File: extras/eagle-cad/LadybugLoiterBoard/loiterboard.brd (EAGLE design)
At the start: 27.5 x 48 mm, 7 parts

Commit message: More LadybugFC loiterboard work
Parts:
- added SMIRF: (no value), SparkFun-Connectors:1X04
- moved LBLFT 11.8 mm to (20.5, 10.0)
- moved LBRGT 11.8 mm to (38.5, 13.0)
- moved PMLFT 11.8 mm to (22.0, 36.3)
- moved PMRGT 11.8 mm to (37.5, 36.3)
- moved PWPWR 11.8 mm to (27.3, 43.8)
- moved VLLFT 11.8 mm to (22.0, 25.9)
- moved VLRGT2 11.8 mm to (37.5, 25.9)
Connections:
- net A4 renamed LED
- removed net TX2/INT: LBLFT.6, VLLFT.3
- new net INT: VLLFT.3
- new net TX2: LBLFT.6, SMIRF.1
- net 5V: now also SMIRF.4
- net GND: now also SMIRF.3
- net RX2: now also SMIRF.2
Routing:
- net TX2: track 0.00 -> 79.6 mm
- net RX2: track 0.00 -> 72.1 mm
- net 5V: track 0.00 -> 71.9 mm
- net TX2/INT: track 31.2 -> 0.00 mm
- net GND: track 1.73 -> 0.12 mm
- removed copper zone on layer 16, net GND
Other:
- board size 27.5 x 48 mm -> 52.1 x 63 mm
- board text added: "5V"
- board text added: "ADD LEDS!"
- board text added: "BLUESMIRF"
- board text added: "CS"
- board text added: "GND"
- board text added: "INT"
- board text added: "LED"
- board text added: "MISO"
- board text added: "MOSI"
- board text added: "RX2"
- board text added: "SCK"
- board text added: "SCL"
- board text added: "SDA"
- board text added: "TX1"
- board text added: "TX2"

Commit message: More Ladybug Loiterboard work
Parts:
- added PAD1, PAD10, PAD2, PAD3, PAD4, PAD5, PAD6, PAD7, PAD8, PAD9: (no value), wirepad:SMD1,27-2,54
- added U$1: 1X2, headers(2mm):1X2
- moved SMIRF 0.75 mm to (50.0, 59.5)
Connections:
- new net VBAT: PAD9.1, U$1.1
- net 5V: now also PAD1.1, PAD3.1, PAD5.1, PAD7.1
- net GND: now also PAD10.1, U$1.2
- net LED: now also PAD2.1, PAD4.1, PAD6.1, PAD8.1
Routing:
- net GND: track 0.12 -> 7.65 mm
- net VBAT: track 0.00 -> 5.22 mm
- net 5V: track 71.9 -> 72.7 mm
- net RX2: track 72.1 -> 72.7 mm
- net TX2: track 79.6 -> 80.2 mm
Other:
- board size 52.1 x 63 mm -> 52.1 x 66.8 mm
- board text added: "VBAT"
- board text removed: "ADD LEDS!"

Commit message: More Ladybug Loiterboard work
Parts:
- moved PAD1 10.8 mm to (15.0, 12.0)
- moved PAD2 10.8 mm to (12.0, 12.0)
- moved PAD5 10.3 mm to (15.0, 39.0)
- moved PAD3 8.81 mm to (49.8, 12.0)
- moved PAD4 8.81 mm to (52.8, 12.0)
- moved PAD6 5.55 mm to (12.0, 39.0)
- moved PAD7 4.51 mm to (49.8, 39.0)
- moved PAD8 4.51 mm to (52.8, 39.0)
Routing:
- net LED: track 0.00 -> 145.1 mm, vias 0 -> 1
- net 5V: track 72.7 -> 141.8 mm, vias 0 -> 1
- net D4/MISO: track 47.1 -> 48.5 mm, vias 0 -> 1
- net SCL: track 17.0 -> 16.4 mm
- net SDA: vias 0 -> 1
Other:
- board size 52.1 x 66.8 mm -> 44.6 x 66.8 mm

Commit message: More Ladybug Loiterboard work
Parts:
- PAD6: value (none) -> LED

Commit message: Completed loiterboard
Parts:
- moved U$1 0.50 mm to (38.5, 4.25)
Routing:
- net VBAT: track 5.22 -> 6.24 mm
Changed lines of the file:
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@@
 <setting verticaltext="up"/>
 </settings>
-<grid distance="0.25" unitdist="mm" unit="mm" style="lines" multiple="1" display="no" altdistance="5" altunitdist="mil" altunit="mil"/>
+<grid distance="0.003125" unitdist="mic" unit="mm" style="lines" multiple="1" display="no" altdistance="5" altunitdist="mil" altunit="mil"/>
 <layers>
 <layer number="1" name="Top" color="4" fill="1" visible="yes" active="yes"/>
@@
 <attribute name="VALUE" x="52.75" y="39" size="0.0254" layer="27"/>
 </element>
-<element name="U$1" library="headers(2mm)" package="1X2" value="1X2" x="38.5" y="3.75" smashed="yes" rot="R270"/>
+<element name="U$1" library="headers(2mm)" package="1X2" value="1X2" x="38.5" y="4.25" smashed="yes" rot="R270"/>
 <element name="PAD9" library="wirepad" package="SMD1,27-2,54" value="" x="43" y="3" smashed="yes" rot="R180">
 <attribute name="VALUE" x="43" y="3" size="0.0254" layer="27" rot="R180"/>
@@
 <contactref element="SMIRF" pad="4"/>
 <wire x1="49.75" y1="51.63" x2="49.75" y2="40.25" width="0.3048" layer="1"/>
-<wire x1="49.75" y1="9.5" x2="46.25" y2="6" width="0.3048" layer="1"/>
-<wire x1="46.25" y1="6" x2="21" y2="6" width="0.3048" layer="1"/>
+<wire x1="49.75" y1="9.5" x2="46.6311875" y2="6.3811875" width="0.3048" layer="1"/>
+<wire x1="46.6311875" y1="6.3811875" x2="20.966846875" y2="6.3811875" width="0.3048" layer="1"/>
 <contactref element="PAD1" pad="1"/>
 <contactref element="PAD3" pad="1"/>
@@
 <wire x1="15" y1="12" x2="15" y2="12.75" width="0" layer="19" extent="1-1"/>
 <wire x1="15" y1="11.25" x2="15" y2="12" width="0" layer="19" extent="1-1"/>
-<wire x1="21" y1="6" x2="20.5" y2="6" width="0" layer="19" extent="1-1"/>
+<wire x1="20.966846875" y1="6.3811875" x2="20.5" y2="6" width="0" layer="19" extent="1-1"/>
 <wire x1="49.75" y1="39" x2="49.75" y2="40.25" width="0" layer="19" extent="1-1"/>
 </signal>
@@
 <contactref element="U$1" pad="2"/>
 <contactref element="PAD10" pad="1"/>
-<wire x1="38.5" y1="2.75" x2="40" y2="1.25" width="0.3048" layer="1"/>
-<wire x1="40" y1="1.25" x2="44" y2="1.25" width="0.3048" layer="1"/>
-<wire x1="44" y1="1.25" x2="45" y2="2.25" width="0.3048" layer="1"/>
-<wire x1="38.5" y1="2.75" x2="38.5" y2="18" width="0" layer="19" extent="1-1"/>
+<wire x1="38.5" y1="3.25" x2="39.98861875" y2="1.265175" width="0.3048" layer="1"/>
+<wire x1="39.98861875" y1="1.265175" x2="44.015175" y2="1.265175" width="0.3048" layer="1"/>
+<wire x1="44.015175" y1="1.265175" x2="45" y2="2.25" width="0.3048" layer="1"/>
+<wire x1="38.456" y1="17.9936" x2="38.5" y2="3.25" width="0" layer="19" extent="1-1"/>
 <wire x1="20.5" y1="16" x2="38.456" y2="17.9936" width="0" layer="19" extent="1-1"/>
 <wire x1="29.82" y1="43.8" x2="22" y2="28.46" width="0" layer="19" extent="1-1"/>
@@
 <contactref element="U$1" pad="1"/>
 <contactref element="PAD9" pad="1"/>
-<wire x1="38.5" y1="4.75" x2="41.25" y2="4.75" width="0.3048" layer="1"/>
-<wire x1="41.25" y1="4.75" x2="43" y2="3" width="0.3048" layer="1"/>
+<wire x1="42.5" y1="3" x2="43" y2="3" width="0.3048" layer="1"/>
+<wire x1="38.5" y1="5.25" x2="40" y2="5.25" width="0.3048" layer="1"/>
+<wire x1="40" y1="5.25" x2="43" y2="2.25" width="0.3048" layer="1"/>
+<wire x1="43" y1="2.25" x2="43" y2="3" width="0" layer="19" extent="1-1"/>
 </signal>
 </signals>

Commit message: Updated Loiterboard
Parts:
- moved SMIRF 2.52 mm to (52.5, 59.5)
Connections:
- net GND: now also U$1.1; no longer U$1.2
- net VBAT: now also U$1.2; no longer U$1.1
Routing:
- net 5V: track 141.6 -> 132.8 mm
- net TX2: track 80.2 -> 82.4 mm
- net RX2: track 72.7 -> 74.9 mm
- net VBAT: track 6.24 -> 5.00 mm

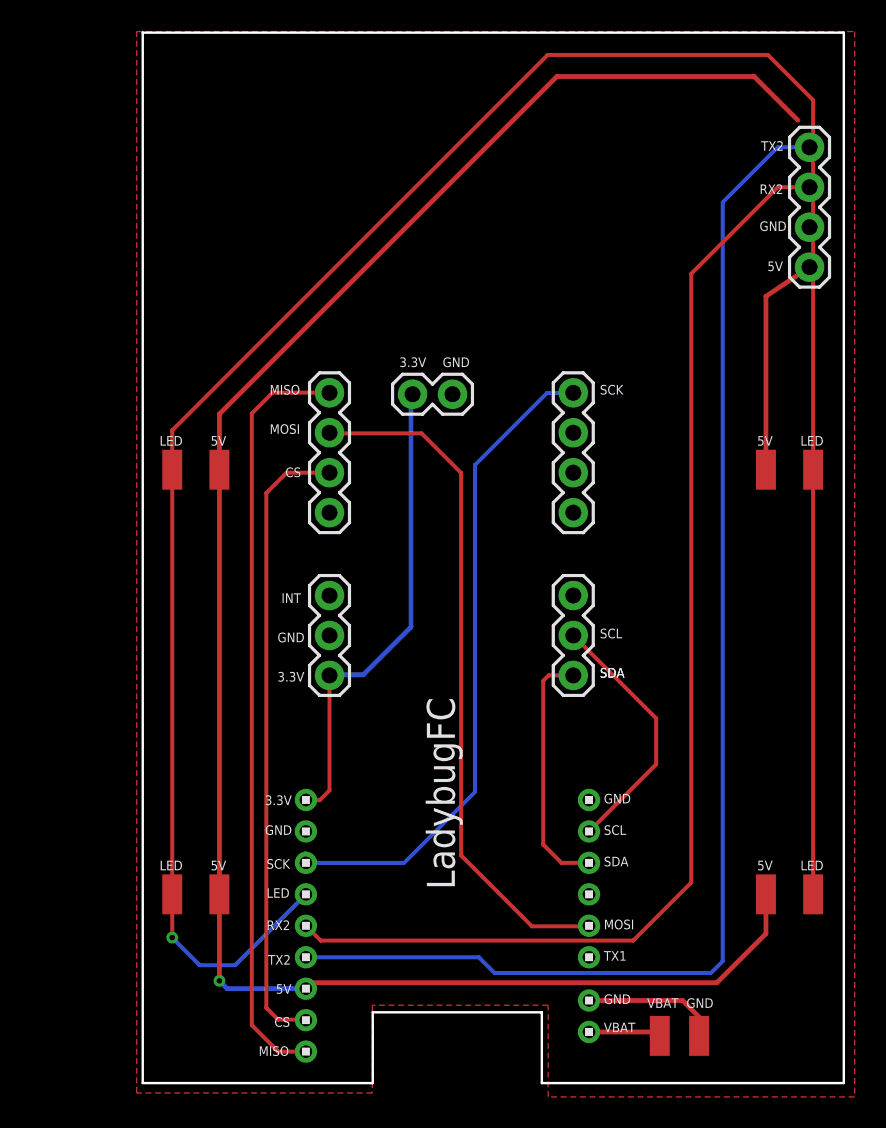
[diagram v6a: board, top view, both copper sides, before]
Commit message: Fixed 5V on loiterboard
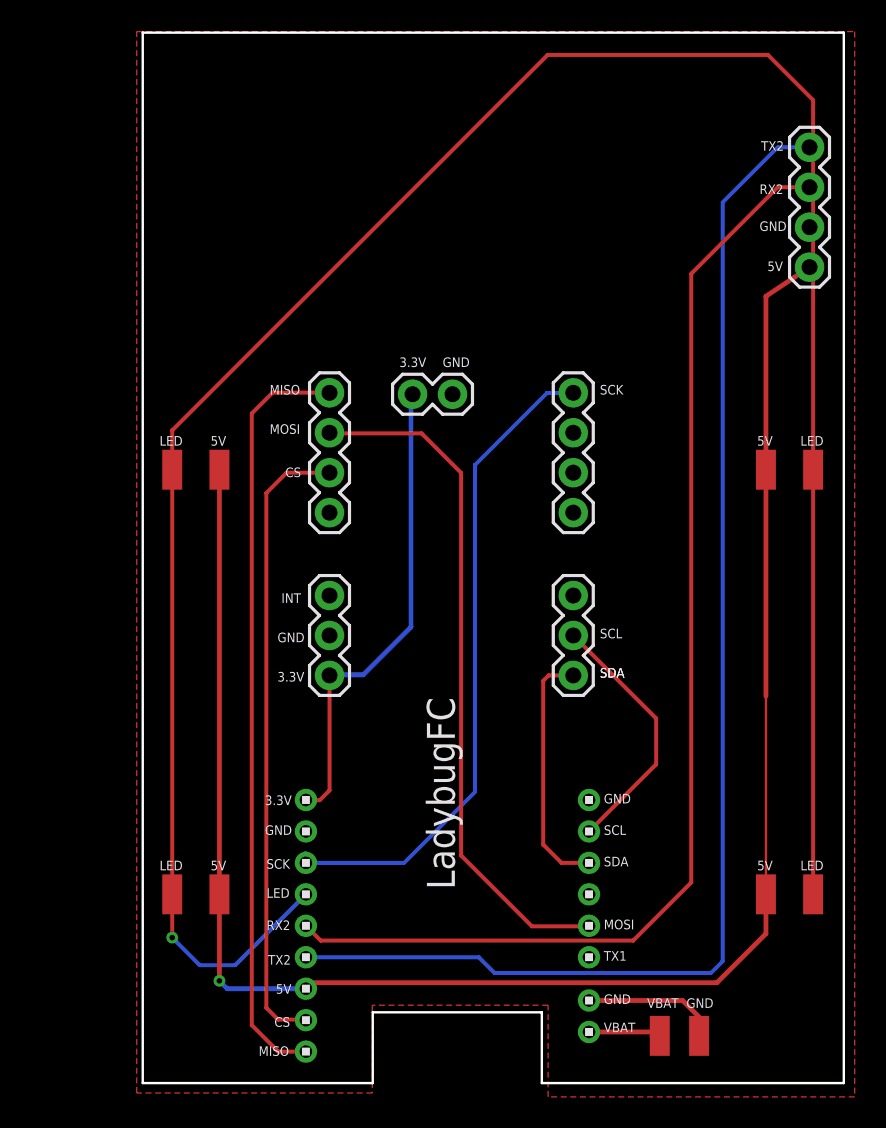
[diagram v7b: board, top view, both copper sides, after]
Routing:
- net 5V: track 132.8 -> 109.4 mm
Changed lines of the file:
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@@
 <contactref element="PAD5" pad="1"/>
 <contactref element="PAD7" pad="1"/>
-<wire x1="36.45763125" y1="64" x2="15" y2="42.54236875" width="0.3048" layer="1"/>
-<wire x1="36.45763125" y1="64" x2="49" y2="64" width="0.3048" layer="1"/>
-<wire x1="49" y1="64" x2="51.78231875" y2="61.21768125" width="0.3048" layer="1"/>
-<wire x1="15" y1="42.54236875" x2="15" y2="39" width="0.3048" layer="1"/>
 <wire x1="15" y1="39" x2="15" y2="12.75" width="0.3048" layer="1"/>
 <wire x1="20.5" y1="6" x2="15.5" y2="6" width="0.3048" layer="16"/>
@@
 <wire x1="49.75" y1="12" x2="49.75" y2="9.5" width="0.3048" layer="1"/>
 <wire x1="49.75" y1="50.025678125" x2="52.521875" y2="51.88" width="0.3048" layer="1"/>
+<wire x1="49.75" y1="39" x2="49.75" y2="24.6" width="0.3048" layer="1"/>
+<wire x1="49.75" y1="24.6" x2="49.75" y2="12" width="0.1524" layer="1"/>
 <wire x1="49.75" y1="39" x2="49.75" y2="40.25" width="0" layer="19" extent="1-1"/>
-<wire x1="51.78231875" y1="61.21768125" x2="52.521875" y2="51.88" width="0" layer="19" extent="1-1"/>
-<wire x1="15" y1="12" x2="15" y2="12.75" width="0" layer="19" extent="1-1"/>
-<wire x1="15" y1="11.25" x2="15" y2="12" width="0" layer="19" extent="1-1"/>
-<wire x1="20.966846875" y1="6.3811875" x2="20.5" y2="6" width="0" layer="19" extent="1-1"/>
+<wire x1="20.5" y1="6" x2="20.966846875" y2="6.3811875" width="0" layer="19" extent="1-1"/>
+<wire x1="15" y1="12" x2="15" y2="11.25" width="0" layer="19" extent="1-1"/>
+<wire x1="15" y1="12.75" x2="15" y2="12" width="0" layer="19" extent="1-1"/>
 </signal>
 <signal name="INT">
@@
 <wire x1="20.5" y1="16" x2="38.456" y2="17.9936" width="0" layer="19" extent="1-1"/>
 <wire x1="29.82" y1="43.8" x2="22" y2="28.46" width="0" layer="19" extent="1-1"/>
+<wire x1="52.521875" y1="54.42" x2="29.82" y2="43.8" width="0" layer="19" extent="1-1"/>
 </signal>
 <signal name="3.3V">

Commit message: More Loiterboard / Haskell Copilot work
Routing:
- net GND: track 7.76 -> 62.6 mm, vias 0 -> 1
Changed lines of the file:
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@@
 <wire x1="38.5" y1="5.25" x2="44.45" y2="5.25" width="0.3048" layer="1"/>
 <wire x1="44.45" y1="5.25" x2="45.7" y2="4" width="0.3048" layer="1"/>
+<wire x1="29.82" y1="43.8" x2="29.82" y2="46.4" width="0.3048" layer="16"/>
+<wire x1="29.82" y1="46.4" x2="29.82" y2="46.58" width="0.3048" layer="16"/>
+<wire x1="29.82" y1="46.58" x2="28.7" y2="47.7" width="0.3048" layer="16"/>
+<wire x1="28.7" y1="47.7" x2="26.1" y2="47.7" width="0.3048" layer="16"/>
+<wire x1="25.1" y1="31.56" x2="22" y2="28.46" width="0.3048" layer="16"/>
+<wire x1="26.1" y1="47.7" x2="25.1" y2="46.7" width="0.3048" layer="16"/>
+<wire x1="25.1" y1="46.7" x2="25.1" y2="31.56" width="0.3048" layer="16"/>
+<wire x1="45.8" y1="48.4" x2="43.8" y2="46.4" width="0.3048" layer="16"/>
+<wire x1="45.8" y1="48.4" x2="45.9424" y2="48.4" width="0.3048" layer="16"/>
+<via x="45.9424" y="48.4" extent="1-16" drill="0.35"/>
+<wire x1="46.2424" y1="48.4" x2="52.2624" y2="54.42" width="0.3048" layer="1"/>
+<wire x1="52.2624" y1="54.42" x2="52.3944" y2="54.42" width="0.1524" layer="1"/>
+<wire x1="43.8" y1="46.4" x2="32.42" y2="46.4" width="0.3048" layer="16"/>
+<wire x1="32.42" y1="46.4" x2="29.82" y2="43.8" width="0.3048" layer="16"/>
+<wire x1="45.9424" y1="48.4" x2="46.2424" y2="48.4" width="0.1524" layer="1"/>
 <wire x1="38.5" y1="5.25" x2="38.456" y2="17.9936" width="0" layer="19" extent="1-1"/>
 <wire x1="20.5" y1="16" x2="38.456" y2="17.9936" width="0" layer="19" extent="1-1"/>
-<wire x1="29.82" y1="43.8" x2="22" y2="28.46" width="0" layer="19" extent="1-1"/>
-<wire x1="52.521875" y1="54.42" x2="29.82" y2="43.8" width="0" layer="19" extent="1-1"/>
 </signal>
 <signal name="3.3V">
